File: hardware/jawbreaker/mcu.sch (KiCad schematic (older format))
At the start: 119 parts, among them J1 GSG-USB-MICRO-B, P19 SPIFI, P20 GPIO, P21 ANALOG, P22 I2S, P23 VCC, P24 1V8, P25 LPC_ISP, P26 LPC_JTAG, P27 LPC_MISC, P28 SD, P29 CPLD_JTAG, P30 BANK2_AUX, P31 BANK1_AUX, U20 W25Q80BV, U21 TPS62410, U22 GSG-IP4220CZ6, U23 LPC43XXFBD144, U24 GSG-XC2C64A-7VQG100C, X2 MCU_XTAL

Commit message: regulator disconnect jumpers
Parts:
- removed P23: VCC, symbol CONN_3X2
- removed P24: 1V8, symbol CONN_3X2
- added P1: 1V8, symbol CONN_2
- added P3: GND, symbol CONN_2
- added P8: VCC, symbol CONN_2
- gave numbers to parts that had none: 4
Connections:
- net +1.8V: now also P1.1 (P1), P1.2 (PM)
- net GND: now also P3.1 (P1), P3.2 (PM)
- net VCC: now also P8.1 (P1), P8.2 (PM)
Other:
- moved on the sheet: C125, C126, C127, C143, C145, C146, L10, L11, R46, R47, R50, R51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

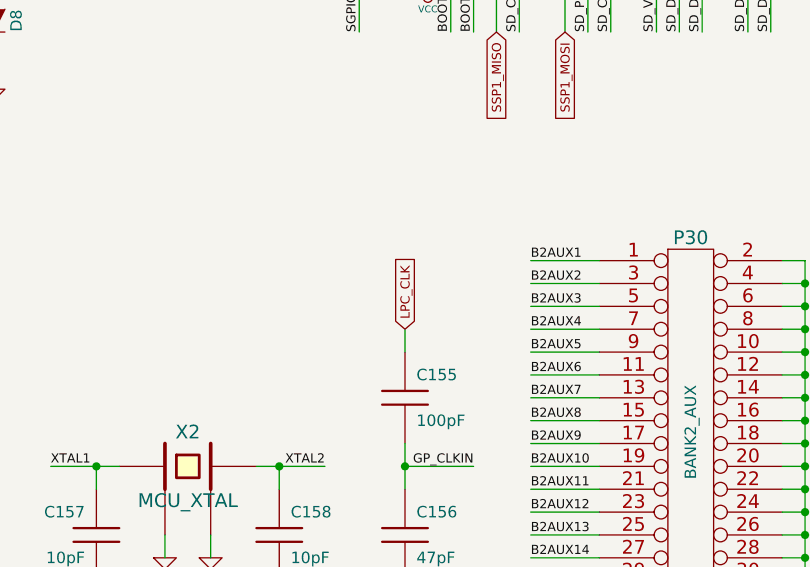
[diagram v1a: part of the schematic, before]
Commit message: MIX_CLK instead of headers
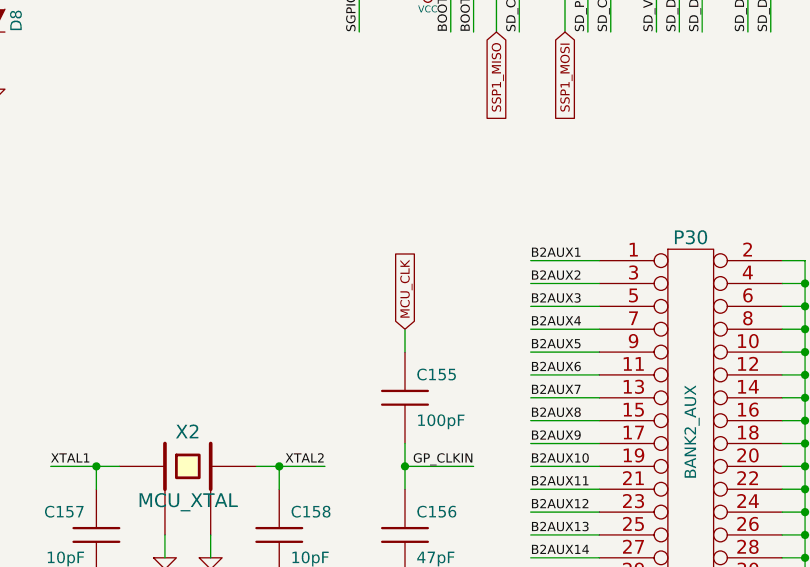
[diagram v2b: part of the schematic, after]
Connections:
- net LPC_CLK renamed MCU_CLK

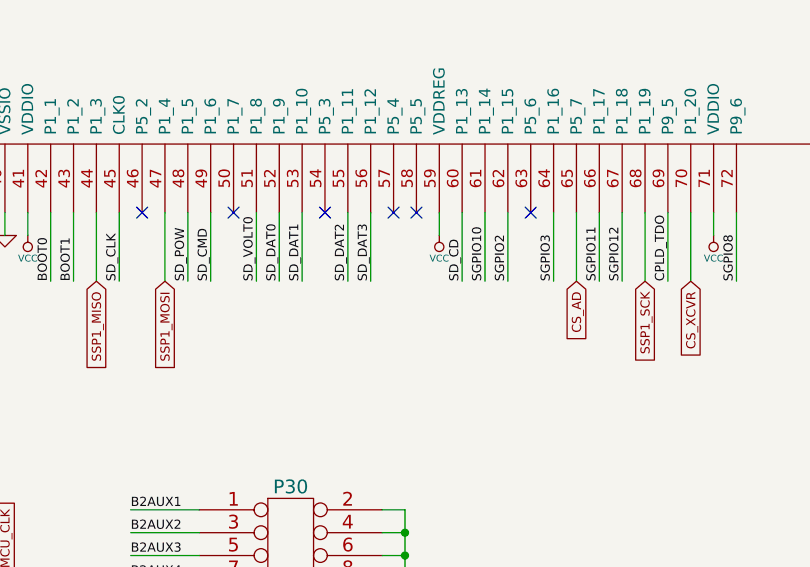
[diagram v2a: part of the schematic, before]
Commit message: mixer control traces instead of headers
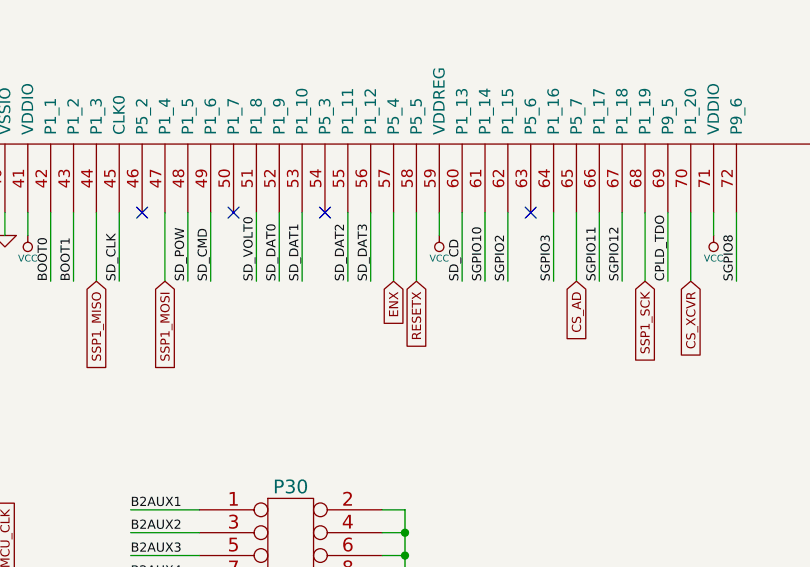
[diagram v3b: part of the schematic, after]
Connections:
- net ENX: now reaches U23.57 (P5_4)
- net RESETX: now reaches U23.58 (P5_5)
- no-connect marks 29 -> 27
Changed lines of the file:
@@
-EESchema Schematic File Version 2  date Sun Sep  2 15:54:35 2012
+EESchema Schematic File Version 2  date Sun Sep  2 16:11:19 2012
 LIBS:power
 LIBS:device
@@
 Comment4 ""
 $EndDescr
+Text GLabel 7350 7750 3    40   Input ~ 0
+RESETX
+Text GLabel 7250 7750 3    40   Input ~ 0
+ENX
+Wire Wire Line
+	7350 7450 7350 7750
 Wire Wire Line
 	15250 3400 15250 3300
@@
 Wire Wire Line
 	15050 3400 15050 3300
+Wire Wire Line
+	7250 7450 7250 7750
 $Comp
 L GND #PWR215
@@
 $EndComp
 NoConn ~ 7850 7450
-NoConn ~ 7350 7450
-NoConn ~ 7250 7450
 NoConn ~ 6950 7450
 NoConn ~ 6150 7450

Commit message: PCB antenna
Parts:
- P20: symbol CONN_8X2 -> CONN_5X2
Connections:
- net GND: now also P20.10; no longer P20.1, P20.11, P20.13, P20.15, P20.3, P20.5, P20.7
- net GPIO3_10: now also P20.3; no longer P20.6
- net GPIO3_11: now also P20.4; no longer P20.8
- net GPIO3_12: now also P20.5; no longer P20.10
- net GPIO3_13: now also P20.6; no longer P20.12
- net GPIO3_14: now also P20.7; no longer P20.14
- net GPIO3_15: now also P20.8; no longer P20.16
- net GPIO3_8: now also P20.1; no longer P20.2
- net GPIO3_9: now also P20.2; no longer P20.4
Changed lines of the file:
@@
-EESchema Schematic File Version 2  date Sun Sep  2 16:11:19 2012
+EESchema Schematic File Version 2  date Mon Sep  3 16:18:00 2012
 LIBS:power
 LIBS:device
@@
 Sheet 4 4
 Title "jawbreaker mcu/usb/power"
-Date "2 sep 2012"
+Date "3 sep 2012"
 Rev ""
 Comp "Copyright 2012 Michael Ossmann"
@@
 Comment4 ""
 $EndDescr
-Text GLabel 7350 7750 3    40   Input ~ 0
-RESETX
-Text GLabel 7250 7750 3    40   Input ~ 0
-ENX
+Wire Wire Line
+	2650 2000 2950 2000
+Wire Wire Line
+	2650 1800 2950 1800
+Wire Wire Line
+	4050 1700 3750 1700
+Wire Wire Line
+	4050 1900 3750 1900
+Wire Wire Line
+	3850 2200 3850 2100
+Wire Wire Line
+	3850 2100 3750 2100
 Wire Wire Line
 	7350 7450 7350 7750
@@
 Wire Wire Line
 	5350 1750 5350 2050
-Connection ~ 2850 2250
-Wire Wire Line
-	2950 2250 2850 2250
-Connection ~ 2850 2050
-Wire Wire Line
-	2850 2050 2950 2050
-Connection ~ 2850 1850
-Wire Wire Line
-	2850 1850 2950 1850
-Connection ~ 2850 1650
-Wire Wire Line
-	2850 1650 2950 1650
-Wire Wire Line
-	3750 2250 4050 2250
-Wire Wire Line
-	3750 2050 4050 2050
-Wire Wire Line
-	3750 1850 4050 1850
-Wire Wire Line
-	3750 1650 4050 1650
 Wire Wire Line
 	8150 2050 8150 1750
@@
 	8350 2050 8350 1750
 Wire Wire Line
-	3750 1550 4050 1550
-Wire Wire Line
-	3750 1750 4050 1750
-Wire Wire Line
-	3750 1950 4050 1950
-Wire Wire Line
-	3750 2150 4050 2150
-Wire Wire Line
-	2850 2350 2850 1550
-Wire Wire Line
-	2850 1550 2950 1550
-Wire Wire Line
-	2850 1750 2950 1750
-Connection ~ 2850 1750
-Wire Wire Line
-	2850 1950 2950 1950
-Connection ~ 2850 1950
-Wire Wire Line
-	2850 2150 2950 2150
-Connection ~ 2850 2150
-Wire Wire Line
 	5450 2050 5450 1750
 Wire Wire Line
@@
 Wire Wire Line
 	7250 7450 7250 7750
+Wire Wire Line
+	2850 2200 2850 2100
+Wire Wire Line
+	2850 2100 2950 2100
+Wire Wire Line
+	3750 2000 4050 2000
+Wire Wire Line
+	3750 1800 4050 1800
+Wire Wire Line
+	2950 1700 2650 1700
+Wire Wire Line
+	2950 1900 2650 1900
+$Comp
+L GND #PWR?
+U 1 1 5043DA37
+P 2850 2200
+F 0 "#PWR?" H 2850 2200 30  0001 C CNN
+F 1 "GND" H 2850 2130 30  0001 C CNN
+	1    2850 2200
+	1    0    0    -1
+$EndComp
+$Comp
+L GND #PWR?
+U 1 1 5043DA33
+P 3850 2200
+F 0 "#PWR?" H 3850 2200 30  0001 C CNN
+F 1 "GND" H 3850 2130 30  0001 C CNN
+	1    3850 2200
+	1    0    0    -1
+$EndComp
+Text Label 2650 1700 0    40   ~ 0
+GPIO3_8
+Text GLabel 7350 7750 3    40   Input ~ 0
+RESETX
+Text GLabel 7250 7750 3    40   Input ~ 0
+ENX
 $Comp
 L GND #PWR215
@@
 Text Label 4000 3500 0    40   ~ 0
 ADC0_0
-$Comp
-L GND #PWR202
-U 1 1 4F8381B1
-P 2850 2350
-F 0 "#PWR202" H 2850 2350 30  0001 C CNN
-F 1 "GND" H 2850 2280 30  0001 C CNN
-	1    2850 2350
-	1    0    0    -1
-$EndComp
-Text Label 4050 2250 2    40   ~ 0
+Text Label 4050 2000 2    40   ~ 0
 GPIO3_15
-Text Label 4050 2150 2    40   ~ 0
+Text Label 2650 2000 0    40   ~ 0
 GPIO3_14
-Text Label 4050 2050 2    40   ~ 0
+Text Label 4050 1900 2    40   ~ 0
 GPIO3_13
-Text Label 4050 1950 2    40   ~ 0
+Text Label 2650 1900 0    40   ~ 0
 GPIO3_12
-Text Label 4050 1850 2    40   ~ 0
+Text Label 4050 1800 2    40   ~ 0
 GPIO3_11
-Text Label 4050 1750 2    40   ~ 0
+Text Label 2650 1800 0    40   ~ 0
 GPIO3_10
-Text Label 4050 1650 2    40   ~ 0
+Text Label 4050 1700 2    40   ~ 0
 GPIO3_9
-Text Label 4050 1550 2    40   ~ 0
-GPIO3_8
-$Comp
-L CONN_8X2 P20
+$Comp
+L CONN_5X2 P20
 U 1 1 4F838167
 P 3350 1900
-F 0 "P20" H 3350 2350 60  0000 C CNN
+F 0 "P20" H 3350 2200 60  0000 C CNN
 F 1 "GPIO" V 3350 1900 50  0000 C CNN
-F 4 "DNP" H 3350 1400 60  0000 C CNN "Note"
+F 4 "DNP" H 3350 1600 60  0000 C CNN "Note"
 	1    3350 1900
 	1    0    0    -1

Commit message: removed series resistors from codec side of CPLD, added to SGPIO side
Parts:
- removed R101, R102: 39, symbol R
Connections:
- net BANK1F4M7 is gone; now on net DA1: U24.42 (BANK1F4M7)
- net BANK1F4M8 is gone; now on net DA0: U24.43 (BANK1F4M8)
- net DA2: now also U24.41 (BANK1F4M6); no longer R100.2
- net DA3: now also U24.40 (BANK1F4M5); no longer R99.2
- net DA4: now also U24.39 (BANK1F4M4); no longer R98.2
- net DA5: now also U24.37 (BANK1F4M3); no longer R97.2
- net DA6: now also U24.36 (BANK1F4M2); no longer R96.2
- net DA7: now also U24.35 (BANK1F4M1); no longer R91.2
- net DD0: now also U24.34 (BANK1F2M16); no longer R90.2
- net DD1: now also U24.33 (BANK1F2M15); no longer R89.2
- net DD2: now also U24.32 (BANK1F2M14); no longer R88.2
- net DD3: now also U24.30 (BANK1F2M13); no longer R87.2
- net DD4: now also U24.29 (BANK1F2M12); no longer R86.2
- net DD5: now also U24.28 (BANK1F2M11); no longer R81.2
- net DD6: now also U24.24 (BANK1F2M9); no longer R80.2
- net DD7: now also U24.19 (BANK1F2M6); no longer R79.2
- net DD8: now also U24.18 (BANK1F2M5); no longer R78.2
- net DD9: now also U24.17 (BANK1F2M4); no longer R77.2
- net SGPIO0: now also R79.1; no longer U24.89 (BANK2F3M3)
- net SGPIO1: now also R81.1; no longer U24.79 (BANK2F3M5)
- net SGPIO10: now also R88.1; no longer U24.76 (BANK2F3M8)
- net SGPIO11: now also R91.1; no longer U24.71 (BANK2F3M11)
- net SGPIO12: now also R96.1; no longer U24.70 (BANK2F3M12)
- net SGPIO13: now also R78.1; no longer U24.90 (BANK2F3M2)
- net SGPIO14: now also R80.1; no longer U24.81 (BANK2F3M4)
- net SGPIO15: now also R86.1; no longer U24.78 (BANK2F3M6)
- net SGPIO2: now also R89.1; no longer U24.74 (BANK2F3M9)
- net SGPIO3: now also R90.1; no longer U24.72 (BANK2F3M10)
- net SGPIO4: now also R98.1; no longer U24.67 (BANK2F3M14)
- net SGPIO5: now also R99.1; no longer U24.64 (BANK2F3M15)
- net SGPIO6: now also R100.1; no longer U24.61 (BANK2F3M16)
- net SGPIO7: now also R87.1; no longer U24.77 (BANK2F3M7)
- net SGPIO8: now also R97.1; no longer U24.68 (BANK2F3M13)
- net SGPIO9: now also R77.1; no longer U24.91 (BANK2F3M1)
- removed net BANK1F2M11: R81.1, U24.28 (BANK1F2M11)
- removed net BANK1F2M12: R86.1, U24.29 (BANK1F2M12)
- removed net BANK1F2M13: R87.1, U24.30 (BANK1F2M13)
- removed net BANK1F2M14: R88.1, U24.32 (BANK1F2M14)
- removed net BANK1F2M15: R89.1, U24.33 (BANK1F2M15)
- removed net BANK1F2M16: R90.1, U24.34 (BANK1F2M16)
- removed net BANK1F2M4: R77.1, U24.17 (BANK1F2M4)
- removed net BANK1F2M5: R78.1, U24.18 (BANK1F2M5)
- removed net BANK1F2M6: R79.1, U24.19 (BANK1F2M6)
- removed net BANK1F2M9: R80.1, U24.24 (BANK1F2M9)
- removed net BANK1F4M1: R91.1, U24.35 (BANK1F4M1)
- removed net BANK1F4M2: R96.1, U24.36 (BANK1F4M2)
- removed net BANK1F4M3: R97.1, U24.37 (BANK1F4M3)
- removed net BANK1F4M4: R98.1, U24.39 (BANK1F4M4)
- removed net BANK1F4M5: R99.1, U24.40 (BANK1F4M5)
- removed net BANK1F4M6: R100.1, U24.41 (BANK1F4M6)
- new net BANK2F3M1: R77.2, U24.91 (BANK2F3M1)
- new net BANK2F3M10: R90.2, U24.72 (BANK2F3M10)
- new net BANK2F3M11: R91.2, U24.71 (BANK2F3M11)
- new net BANK2F3M12: R96.2, U24.70 (BANK2F3M12)
- new net BANK2F3M13: R97.2, U24.68 (BANK2F3M13)
- new net BANK2F3M14: R98.2, U24.67 (BANK2F3M14)
- new net BANK2F3M15: R99.2, U24.64 (BANK2F3M15)
- new net BANK2F3M16: R100.2, U24.61 (BANK2F3M16)
- new net BANK2F3M2: R78.2, U24.90 (BANK2F3M2)
- new net BANK2F3M3: R79.2, U24.89 (BANK2F3M3)
- new net BANK2F3M4: R80.2, U24.81 (BANK2F3M4)
- new net BANK2F3M5: R81.2, U24.79 (BANK2F3M5)
- new net BANK2F3M6: R86.2, U24.78 (BANK2F3M6)
- new net BANK2F3M7: R87.2, U24.77 (BANK2F3M7)
- new net BANK2F3M8: R88.2, U24.76 (BANK2F3M8)
- new net BANK2F3M9: R89.2, U24.74 (BANK2F3M9)
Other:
- note added: "Series resistors are here because of a possible\novershoot/undershoot problem. They may be able to be removed\nsafely. Anyway, they probably will minimize damage in the event of\nSGPIO/CPLD misconfiguration."
- moved on the sheet: R100, R77, R78, R79, R80, R81, R86, R87, R88, R89, R90, R91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

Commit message: reduced expansion headers to save space
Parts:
- removed P22: I2S, symbol CONN_5X2
- removed P27: LPC_MISC, symbol CONN_12X2
- removed P30: BANK2_AUX, symbol CONN_16X2
- removed P31: BANK1_AUX, symbol CONN_8X2
- added P10: CTOUT_2, symbol CONN_1
- added P11: CTIN_2, symbol CONN_1
- added P12: U3_RXD, symbol CONN_1
- added P13: U3_TXD, symbol CONN_1
- added P22: I2S, symbol CONN_3X2
- added P23: DBGEN, symbol CONN_1
- added P24: TRST, symbol CONN_1
- added P30: BANK2_AUX, symbol CONN_8X2
- added P31: BANK1_AUX, symbol CONN_5X2
- added P5: WAKEUP, symbol CONN_1
- added P6: TRACECLK, symbol CONN_1
- added P7: CTIN_4, symbol CONN_1
- added P9: CTOUT_4, symbol CONN_1
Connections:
- net B1AUX10: now also P31.2
- net B1AUX11: now also P31.3
- net B1AUX12: now also P31.4
- net B1AUX13: now also P31.5
- net B1AUX14: now also P31.6
- net B1AUX15: now also P31.7
- net B1AUX16: now also P31.8
- net B1AUX9: now also P31.1
- net B2AUX1: now also P30.1
- net B2AUX10: now also P30.10
- net B2AUX11: now also P30.11
- net B2AUX12: now also P30.12
- net B2AUX13: now also P30.13
- net B2AUX14: now also P30.14
- net B2AUX15: now also P30.15
- net B2AUX16: now also P30.16
- net B2AUX2: now also P30.2
- net B2AUX3: now also P30.3
- net B2AUX4: now also P30.4
- net B2AUX5: now also P30.5
- net B2AUX6: now also P30.6
- net B2AUX7: now also P30.7
- net B2AUX8: now also P30.8
- net B2AUX9: now also P30.9
- net DBGEN: now also P23.1
- net GND: now also P22.6, P31.10, P31.9
- net I2S0_TX_MCLK: now also P22.5
- net I2S0_TX_SCK: now also P22.4
- net I2S0_TX_SDA: now also P22.2
- net I2S0_TX_WS: now also P22.3
- net VCC: now also P22.1
- net CTIN_2: no longer names the net of U23.91 (P2_5)
- net CTIN_2: now also P11.1
- net CTIN_4: no longer names the net of U23.108 (P2_13)
- net CTIN_4: now also P7.1
- net CTOUT_2: no longer names the net of U23.104 (P2_10)
- net CTOUT_2: now also P10.1
- net CTOUT_4: no longer names the net of U23.106 (P2_12)
- net CTOUT_4: now also P9.1
- net CTOUT_5: no longer names the net of U23.105 (P2_11)
- net TRACECLK: no longer names the net of U23.120 (PF_4)
- net TRACECLK: now also P6.1
- net TRST: no longer names the net of U23.29 (TRST)
- net TRST: now also P24.1
- net U3_RXD: no longer names the net of U23.88 (P2_4)
- net U3_RXD: now also P12.1
- net U3_TXD: no longer names the net of U23.87 (P2_3)
- net U3_TXD: now also P13.1
- net WAKEUP: no longer names the net of R48.2, U23.130 (WAKEUP0)
- net WAKEUP: now also P5.1
- no-connect marks 27 -> 28
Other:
- moved on the sheet: D4, D5, D6, D7, D8, P28, R72, R73, R74, R75, R76

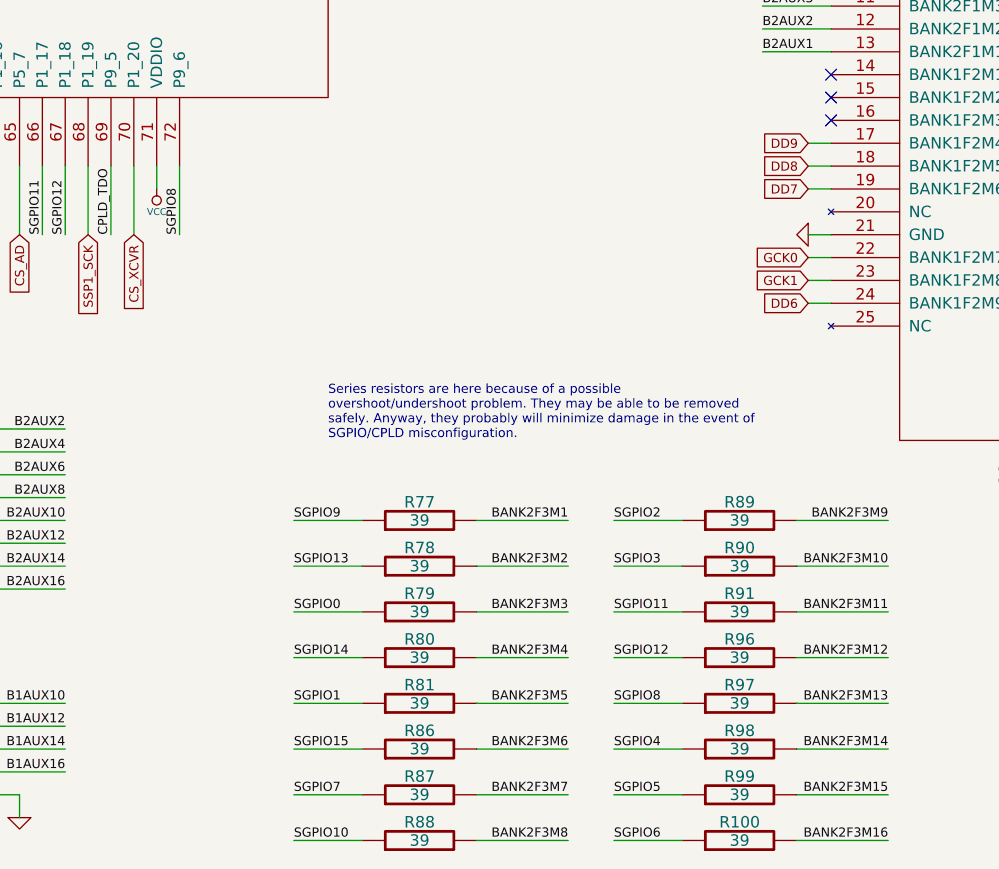
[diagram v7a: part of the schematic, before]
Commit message: updated clocking scheme
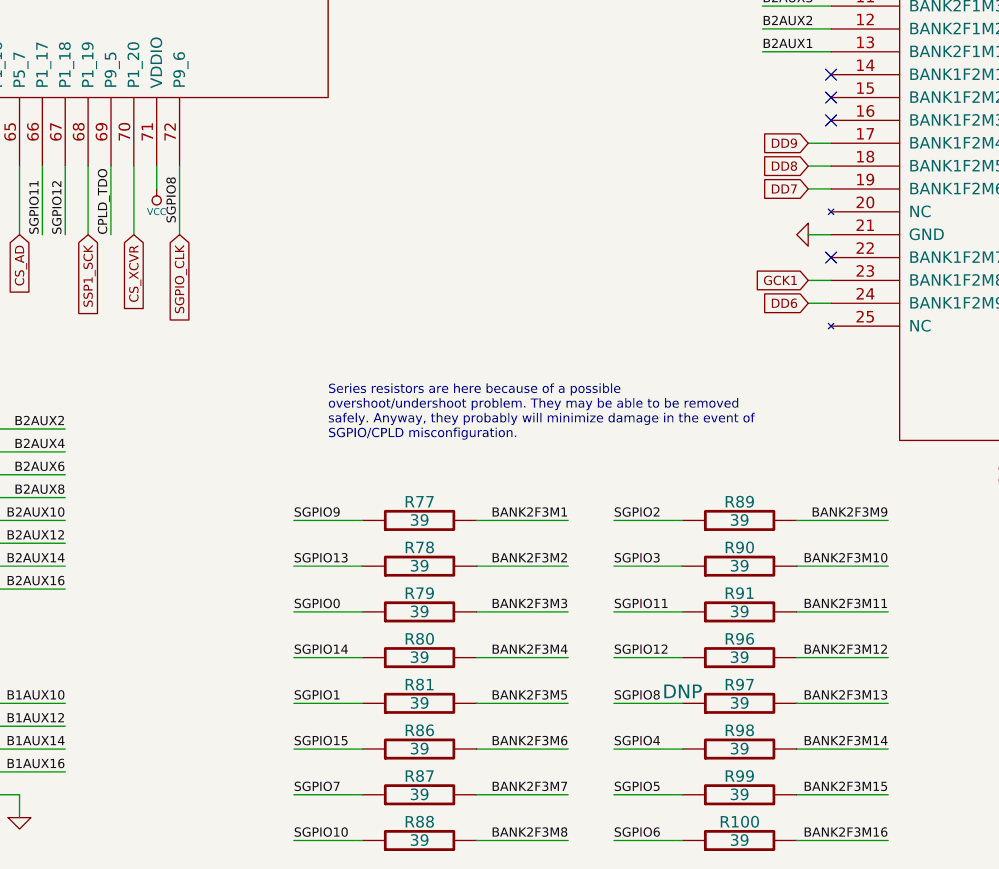
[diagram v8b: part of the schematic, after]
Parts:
- R97: Note (none) -> DNP
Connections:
- net GCK0: no longer names the net of U24.22 (BANK1F2M7)
- net SGPIO8 renamed SGPIO_CLK
- no-connect marks 28 -> 29
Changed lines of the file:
@@
-EESchema Schematic File Version 2  date Mon Sep  3 22:23:28 2012
+EESchema Schematic File Version 2  date Tue Sep  4 10:12:04 2012
 LIBS:power
 LIBS:device
@@
 Comment4 ""
 $EndDescr
+Text GLabel 8750 7750 3    40   Input ~ 0
+SGPIO_CLK
+NoConn ~ 11600 7850
 $Comp
 L CONN_1 P11
@@
 	12500 8950 12500 9050
 Wire Wire Line
-	11600 7850 11500 7850
-Wire Wire Line
 	2700 4350 2700 4250
 Wire Wire Line
@@
 F 5 "RMCF0402JT39R0" H 11200 9800 60  0001 C CNN "Part Number"
 F 6 "RES 39 OHM 1/16W 5% 0402 SMD" H 11200 9800 60  0001 C CNN "Description"
+F 7 "DNP" V 11250 10050 60  0000 C CNN "Note"
 	1    11200 9800
 	0    -1   -1   0
@@
 Text GLabel 4200 3100 0    40   Input ~ 0
 RSSI
-Text GLabel 11500 7850 0    40   Input ~ 0
-GCK0
 Text Label 9250 9400 0    40   ~ 0
 SGPIO0
@@
 Text Label 4000 3600 0    40   ~ 0
 SGPIO9
-Text Label 8750 7750 1    40   ~ 0
+Text Label 8750 7700 1    40   ~ 0
 SGPIO8
 Text Label 7050 7750 1    40   ~ 0
